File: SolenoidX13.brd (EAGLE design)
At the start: 24.3 x 25.4 mm, 23 parts, among them U1 ULN2003V12

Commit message: big pog uwu
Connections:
- net SWCLK: now also STM.PA14; no longer STM.PA13
- net SWDIO: now also STM.PA13; no longer STM.PA14
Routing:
- net SWDIO: track 41.8 -> 43.2 mm
- net SWCLK: track 34.1 -> 34.8 mm
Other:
- board text added: "+3.3v"
- board text added: "GND"
- board text added: "NRST"
- board text added: "SWCLK"
- board text added: "SWDIO"
- board text added: "X13 Solenoid 5/14/21 Erin Park Katherine Sandys Grant Geyer"
- board text removed: "X13 Solenoid 01/01/2021 Erin Park Katherine Sandys Grant Geyer"
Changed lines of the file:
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@@
 3.3V
 STM</text>
-<text x="14.5288" y="0.6096" size="0.6096" layer="25">X13 Solenoid
-01/01/2021
+<text x="13.8938" y="0.4826" size="0.6096" layer="25">X13 Solenoid
+5/14/21
 Erin Park
 Katherine Sandys
@@
 <rectangle x1="17.789525" y1="9.336403125" x2="17.98764375" y2="9.352915625" layer="200"/>
 <rectangle x1="17.822546875" y1="9.352915625" x2="17.954621875" y2="9.369421875" layer="200"/>
+<text x="18.8468" y="0.6096" size="0.6096" layer="25">+3.3v</text>
+<text x="17.7038" y="3.2766" size="0.6096" layer="25">SWCLK</text>
+<text x="18.5928" y="5.9436" size="0.6096" layer="25">GND</text>
+<text x="17.7038" y="8.6106" size="0.6096" layer="25">SWDIO</text>
+<text x="18.3388" y="10.8966" size="0.6096" layer="25">NRST</text>
 </plain>
 <attributes>
@@
 <attribute name="MF" value="" x="22.0472" y="6.2738" size="1.778" layer="27" rot="R270" display="off"/>
 <attribute name="MPN" value="" x="22.0472" y="6.2738" size="1.778" layer="27" rot="R270" display="off"/>
-<attribute name="NAME" x="19.7866" y="11.4808" size="0.8128" layer="25" ratio="10" rot="R270"/>
+<attribute name="NAME" x="18.3642" y="11.7856" size="0.8128" layer="25" ratio="10"/>
 <attribute name="OC_FARNELL" value="unknown" x="22.0472" y="6.2738" size="1.778" layer="27" rot="R270" display="off"/>
 <attribute name="OC_NEWARK" value="unknown" x="22.0472" y="6.2738" size="1.778" layer="27" rot="R270" display="off"/>
@@
 <via x="19.1798" y="10.414" extent="1-16" drill="0.35"/>
 <via x="14.176" y="4.0386" extent="1-16" drill="0.35"/>
-<via x="15.827" y="9.4742" extent="1-16" drill="0.35"/>
+<via x="16.208" y="9.2202" extent="1-16" drill="0.35"/>
 <via x="6.8862" y="6.5024" extent="1-16" drill="0.35"/>
 <contactref element="RESET" pad="1"/>
@@
 <wire x1="22.0472" y1="8.7982125" x2="15.5444" y2="2.2954125" width="0.254" layer="1"/>
 <wire x1="22.0472" y1="8.8138" x2="22.0472" y2="8.7982125" width="0.254" layer="1"/>
-<wire x1="22.0472" y1="8.8138" x2="22.0472" y2="8.9408" width="0.254" layer="1"/>
-<wire x1="19.4474" y1="11.5406" x2="22.0472" y2="8.9408" width="0.254" layer="1"/>
 <contactref element="U$1" pad="13"/>
 <wire x1="0.4826" y1="10.1854" x2="1.1572" y2="10.86" width="0.2032" layer="16"/>
 <wire x1="1.1572" y1="10.86" x2="2.286" y2="10.86" width="0.2032" layer="16"/>
-<contactref element="STM" pad="PA14"/>
-<wire x1="17.6142" y1="11.5406" x2="19.4474" y2="11.5406" width="0.254" layer="1"/>
+<contactref element="STM" pad="PA13"/>
+<wire x1="16.8142" y1="11.5406" x2="16.8142" y2="10.7448" width="0.254" layer="1"/>
+<wire x1="19.177" y1="9.144" x2="19.431" y2="9.398" width="0.254" layer="1"/>
+<wire x1="19.431" y1="9.398" x2="21.463" y2="9.398" width="0.254" layer="1"/>
+<wire x1="21.463" y1="9.398" x2="22.0472" y2="8.8138" width="0.254" layer="1"/>
+<wire x1="16.8142" y1="10.7448" x2="18.415" y2="9.144" width="0.254" layer="1"/>
+<wire x1="18.415" y1="9.144" x2="19.177" y2="9.144" width="0.254" layer="1"/>
 </signal>
 <signal name="SWCLK">
 <contactref element="SV1" pad="4"/>
-<via x="17.442890625" y="10.381690625" extent="1-16" drill="0.35"/>
-<wire x1="17.442890625" y1="10.381690625" x2="17.2692" y2="10.208" width="0.2032" layer="16"/>
 <via x="10.318" y="9.7076875" extent="1-16" drill="0.35"/>
 <wire x1="12.525" y1="10.5636" x2="11.9359125" y2="10.5636" width="0.2032" layer="16"/>
 <wire x1="11.9359125" y1="10.5636" x2="11.08" y2="9.7076875" width="0.2032" layer="16"/>
 <wire x1="11.08" y1="9.7076875" x2="10.318" y2="9.7076875" width="0.2032" layer="16"/>
-<wire x1="17.2692" y1="10.208" x2="12.8806" y2="10.208" width="0.2032" layer="16"/>
-<wire x1="12.8806" y1="10.208" x2="12.525" y2="10.5636" width="0.2032" layer="16"/>
+<wire x1="17.2692" y1="10.589" x2="16.6342" y2="9.954" width="0.2032" layer="16"/>
+<wire x1="16.6342" y1="9.954" x2="13.1346" y2="9.954" width="0.2032" layer="16"/>
+<wire x1="13.1346" y1="9.954" x2="12.525" y2="10.5636" width="0.2032" layer="16"/>
 <wire x1="10.318" y1="9.7076875" x2="9.1488875" y2="9.7076875" width="0.2032" layer="1"/>
 <wire x1="9.1488875" y1="9.7076875" x2="7.2898" y2="7.8486" width="0.2032" layer="1"/>
-<wire x1="17.442890625" y1="10.381690625" x2="20.4216" y2="7.40298125" width="0.254" layer="16"/>
 <wire x1="20.4216" y1="5.3594" x2="22.0472" y2="3.7338" width="0.254" layer="16"/>
-<wire x1="20.4216" y1="7.40298125" x2="20.4216" y2="5.3594" width="0.254" layer="16"/>
+<wire x1="20.4216" y1="5.3594" x2="20.4216" y2="8.16498125" width="0.254" layer="16"/>
 <contactref element="U$1" pad="11"/>
 <wire x1="7.2898" y1="7.8486" x2="1.1684" y2="7.8486" width="0.2032" layer="1"/>
@@
 <wire x1="1.43" y1="12.86" x2="2.286" y2="12.86" width="0.2032" layer="1"/>
 <wire x1="0.508" y1="11.938" x2="1.43" y2="12.86" width="0.2032" layer="1"/>
-<contactref element="STM" pad="PA13"/>
-<wire x1="16.8142" y1="11.5406" x2="16.8142" y2="11.01038125" width="0.254" layer="1"/>
-<wire x1="16.8142" y1="11.01038125" x2="17.442890625" y2="10.381690625" width="0.254" layer="1"/>
+<contactref element="STM" pad="PA14"/>
+<wire x1="20.4216" y1="8.16498125" x2="18.12458125" y2="10.462" width="0.254" layer="16"/>
+<wire x1="18.12458125" y1="10.462" x2="17.99758125" y2="10.589" width="0.2032" layer="16"/>
+<wire x1="17.99758125" y1="10.589" x2="17.2692" y2="10.589" width="0.2032" layer="16"/>
+<wire x1="17.6142" y1="11.5406" x2="17.7412" y2="11.4136" width="0.254" layer="1"/>
+<wire x1="17.7412" y1="11.4136" x2="17.7412" y2="10.84538125" width="0.254" layer="1"/>
+<wire x1="18.12458125" y1="10.462" x2="17.7412" y2="10.84538125" width="0.254" layer="1"/>
+<via x="18.12458125" y="10.462" extent="1-16" drill="0.35"/>
 </signal>
 <signal name="SOL1_1">

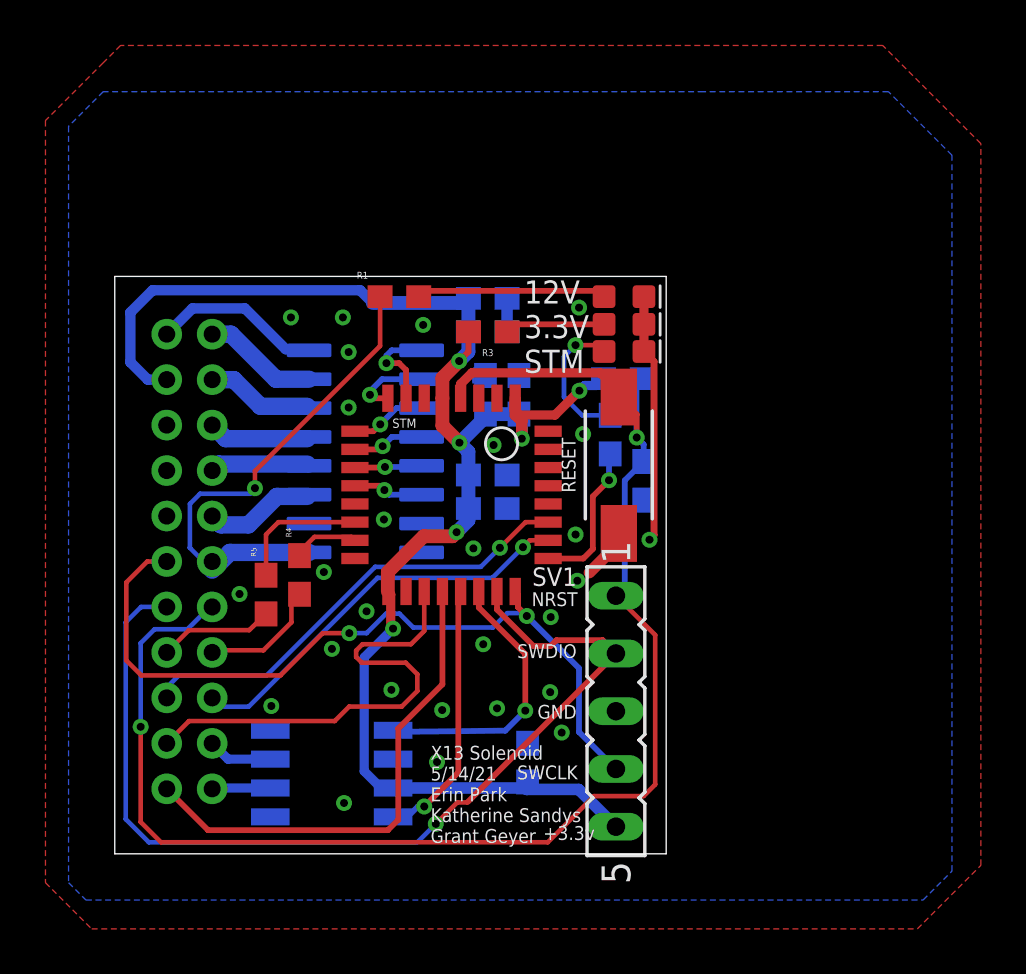
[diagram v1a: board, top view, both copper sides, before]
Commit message: New SWD programming connecotr
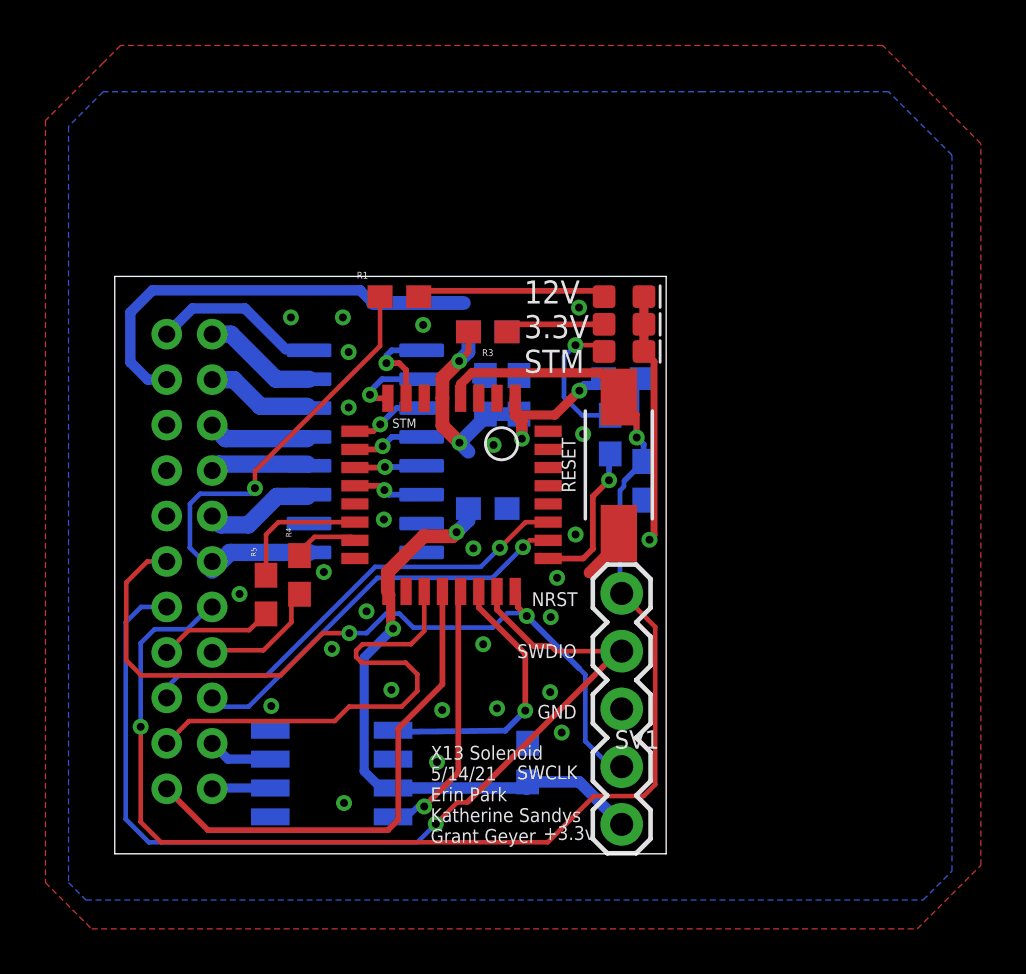
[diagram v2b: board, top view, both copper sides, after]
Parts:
- removed C4, C6: 4.7uF, SparkFun-Capacitors:0603
- C10, C2, C3, C5, C7: value 4.7uF -> 0.1uF
- R2: value 1k -> 10k
- SV1: value (none) -> 3V3 -SWCLK-GND-SWDIO- NRST; device con-lsta:FE05-1 -> CONN, Serial Wire Programming Headers:1X05
- moved SV1 4.98 mm to (22.3, 1.30), turned to 90 degrees
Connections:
- net +3V3: now also SV1.1; no longer C4.1, C6.1, SV1.5
- net GND: no longer C4.2, C6.2
- net NRST: now also SV1.5; no longer SV1.1
- net SWCLK: now also SV1.2; no longer SV1.4
- net SWDIO: now also SV1.4; no longer SV1.2
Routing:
- net +3V3: track 69.0 -> 65.1 mm
- net GND: track 14.7 -> 13.2 mm

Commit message: wack
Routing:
- net +3V3: track 65.1 -> 66.3 mm
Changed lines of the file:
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@@
 </polygon>
 <via x="19.4592" y="12.1412" extent="1-16" drill="0.35"/>
-<via x="19.1798" y="10.414" extent="1-16" drill="0.35"/>
+<via x="20.0688" y="10.287" extent="1-16" drill="0.35"/>
 <via x="14.176" y="4.0386" extent="1-16" drill="0.35"/>
 <via x="16.208" y="9.2202" extent="1-16" drill="0.35"/>
@@
 <via x="11.8392" y="14.7066" extent="1-16" drill="0.35"/>
 <via x="16.6652" y="17.9832" extent="1-16" drill="0.35"/>
-<via x="19.1544" y="7.112" extent="1-16" drill="0.35"/>
+<via x="19.9164" y="7.366" extent="1-16" drill="0.35"/>
 <wire x1="23.2798" y1="22.098" x2="23.7236" y2="21.6542" width="0.3048" layer="1"/>
 <wire x1="22.1742" y1="14.0942" x2="22.1742" y2="13.6652" width="0.3048" layer="1"/>
@@
 <wire x1="23.7236" y1="14.018" x2="23.5232" y2="13.8176" width="0.3048" layer="1"/>
 <wire x1="23.7236" y1="21.6542" x2="23.7236" y2="14.018" width="0.3048" layer="1"/>
-<wire x1="23.2798" y1="24.511" x2="20.4244" y2="24.0284" width="0" layer="19" extent="1-1"/>
-<wire x1="22.1742" y1="14.0942" x2="23.5232" y2="13.8176" width="0" layer="19" extent="1-1"/>
-<wire x1="19.4592" y1="12.1412" x2="20.8788" y2="12.3698" width="0" layer="19" extent="1-1"/>
-<wire x1="23.2664" y1="15.5584" x2="23.5232" y2="13.8176" width="0" layer="19" extent="16-16"/>
-<wire x1="19.1798" y1="10.414" x2="19.4592" y2="12.1412" width="0" layer="19" extent="1-1"/>
-<wire x1="20.272" y1="14.0462" x2="20.8788" y2="12.3698" width="0" layer="19" extent="1-1"/>
-<wire x1="17.2584" y1="15.1892" x2="20.272" y2="14.0462" width="0" layer="19" extent="16-16"/>
-<wire x1="15.7762" y1="13.4366" x2="17.2584" y2="15.1892" width="0" layer="19" extent="16-16"/>
-<wire x1="13.4986" y1="13.2588" x2="15.7762" y2="13.4366" width="0" layer="19" extent="16-16"/>
-<wire x1="11.8392" y1="14.7066" x2="13.4986" y2="13.2588" width="0" layer="19" extent="16-16"/>
-<wire x1="10.5642" y1="12.9906" x2="11.8392" y2="14.7066" width="0" layer="19" extent="1-1"/>
-<wire x1="9.1976" y1="12.3952" x2="10.5642" y2="12.9906" width="0" layer="19" extent="1-1"/>
-<wire x1="11.0772" y1="10.668" x2="10.5642" y2="12.9906" width="0" layer="19" extent="1-1"/>
 <wire x1="9.5532" y1="9.017" x2="11.0772" y2="10.668" width="0" layer="19" extent="1-1"/>
-<wire x1="16.6652" y1="17.9832" x2="17.2584" y2="15.1892" width="0" layer="19" extent="16-16"/>
-<wire x1="19.0642" y1="17.7906" x2="16.6652" y2="17.9832" width="0" layer="19" extent="1-1"/>
-<wire x1="19.0642" y1="18.5906" x2="19.0642" y2="17.7906" width="0" layer="19" extent="1-1"/>
-<wire x1="20.6022" y1="18.4658" x2="19.0642" y2="18.5906" width="0" layer="19" extent="1-1"/>
-<wire x1="17.78" y1="21.043" x2="19.0642" y2="18.5906" width="0" layer="19" extent="1-16"/>
-<wire x1="16.3068" y1="21.043" x2="17.78" y2="21.043" width="0" layer="19" extent="16-16"/>
-<wire x1="17.2584" y1="22.9616" x2="17.78" y2="21.043" width="0" layer="19" extent="16-16"/>
-<wire x1="12.1694" y1="7.2136" x2="9.5532" y2="9.017" width="0" layer="19" extent="1-1"/>
-<wire x1="14.4046" y1="6.3246" x2="12.1694" y2="7.2136" width="0" layer="19" extent="1-1"/>
-<wire x1="14.176" y1="4.0386" x2="14.4046" y2="6.3246" width="0" layer="19" extent="1-1"/>
-<wire x1="12.2428" y1="4.1656" x2="14.176" y2="4.0386" width="0" layer="19" extent="16-16"/>
-<wire x1="16.8176" y1="6.4008" x2="14.4046" y2="6.3246" width="0" layer="19" extent="1-1"/>
-<wire x1="18.161" y1="4.8632" x2="16.8176" y2="6.4008" width="0" layer="19" extent="16-16"/>
-<wire x1="19.6624" y1="5.334" x2="18.161" y2="4.8632" width="0" layer="19" extent="16-16"/>
-<wire x1="19.1544" y1="7.112" x2="19.6624" y2="5.334" width="0" layer="19" extent="1-1"/>
-<wire x1="22.3012" y1="6.3754" x2="19.6624" y2="5.334" width="0" layer="19" extent="1-1"/>
-<wire x1="16.208" y1="9.2202" x2="16.8176" y2="6.4008" width="0" layer="19" extent="1-1"/>
-<wire x1="10.0866" y1="2.2352" x2="12.2428" y2="4.1656" width="0" layer="19" extent="16-16"/>
-<wire x1="13.5664" y1="23.2664" x2="16.3068" y2="21.043" width="0" layer="19" extent="16-16"/>
-<wire x1="10.2898" y1="22.0726" x2="13.5664" y2="23.2664" width="0" layer="19" extent="1-1"/>
-<wire x1="10.0358" y1="23.5966" x2="10.2898" y2="22.0726" width="0" layer="19" extent="1-1"/>
-<wire x1="7.7498" y1="23.5966" x2="10.0358" y2="23.5966" width="0" layer="19" extent="1-1"/>
-<wire x1="10.2898" y1="19.6342" x2="10.2898" y2="22.0726" width="0" layer="19" extent="1-1"/>
-<wire x1="6.8862" y1="6.5024" x2="9.5532" y2="9.017" width="0" layer="19" extent="1-1"/>
-<wire x1="5.4892" y1="11.43" x2="9.1976" y2="12.3952" width="0" layer="19" extent="1-1"/>
-<wire x1="2.286" y1="14.86" x2="5.4892" y2="11.43" width="0" layer="19" extent="1-1"/>
-<wire x1="2.286" y1="16.86" x2="2.286" y2="14.86" width="0" layer="19" extent="1-1"/>
-<wire x1="2.286" y1="18.86" x2="2.286" y2="16.86" width="0" layer="19" extent="1-1"/>
 </signal>
 <signal name="+3V3">
@@
 <via x="20.4401375" y="20.3736" extent="1-16" drill="0.35"/>
 <wire x1="10.795" y1="24.7904" x2="11.3538" y2="24.2316" width="0.4572" layer="16"/>
-<wire x1="11.3538" y1="24.2316" x2="15.3552" y2="24.2316" width="0.6096" layer="16"/>
 <wire x1="1.6628" y1="24.7904" x2="10.795" y2="24.7904" width="0.4572" layer="16"/>
 <wire x1="15.5584" y1="22.9616" x2="15.5584" y2="22.0832125" width="0.6096" layer="16"/>
@@
 <wire x1="0.6858" y1="21.6274" x2="1.4532" y2="20.86" width="0.4572" layer="16"/>
 <wire x1="1.4532" y1="20.86" x2="2.286" y2="20.86" width="0.4572" layer="16"/>
-<wire x1="18.161" y1="3.1632" x2="20.4334" y2="3.1632" width="0.508" layer="16"/>
-<wire x1="20.4334" y1="3.1632" x2="22.3012" y2="1.2954" width="0.508" layer="16"/>
-<wire x1="15.3552" y1="24.2316" x2="15.5584" y2="22.9616" width="0" layer="19" extent="16-16"/>
+<wire x1="18.161" y1="3.1632" x2="19.6714" y2="3.1632" width="0.508" layer="16"/>
+<wire x1="21.5392" y1="1.2954" x2="22.3012" y2="1.2954" width="0.508" layer="16"/>
+<wire x1="21.5392" y1="1.2954" x2="19.6714" y2="3.1632" width="0.508" layer="16"/>
+<wire x1="11.3538" y1="24.2316" x2="11.4554" y2="24.13" width="0.4064" layer="16"/>
+<wire x1="15.5584" y1="23.8116" x2="15.5584" y2="22.9616" width="0.4064" layer="16"/>
+<wire x1="11.4554" y1="24.13" x2="15.24" y2="24.13" width="0.4064" layer="16"/>
+<wire x1="15.24" y1="24.13" x2="15.5584" y2="23.8116" width="0.4064" layer="16"/>
 <wire x1="15.5584" y1="15.1892" x2="15.5584" y2="17.6902" width="0" layer="19" extent="16-16"/>
 </signal>
@@
 <wire x1="13.3124" y1="0.508" x2="14.1224" y2="1.318" width="0.2032" layer="16"/>
 <via x="14.1224" y="1.318" extent="1-16" drill="0.35"/>
-<wire x1="14.1224" y1="1.318" x2="15.0678" y2="2.2634" width="0.2032" layer="1"/>
-<wire x1="15.5123875" y1="2.2634" x2="15.0678" y2="2.2634" width="0.2032" layer="1"/>
-<wire x1="15.5123875" y1="2.2634" x2="15.5444" y2="2.2954125" width="0.2032" layer="1"/>
 <wire x1="0.4826" y1="1.524" x2="0.4826" y2="10.1854" width="0.2032" layer="16"/>
-<wire x1="22.164390625" y1="8.915403125" x2="15.5444" y2="2.2954125" width="0.254" layer="1"/>
-<wire x1="22.3012" y1="8.9154" x2="22.164390625" y2="8.915403125" width="0.254" layer="1"/>
 <contactref element="U$1" pad="13"/>
 <wire x1="0.4826" y1="10.1854" x2="1.1572" y2="10.86" width="0.2032" layer="16"/>
@@
 <contactref element="STM" pad="PA13"/>
 <wire x1="16.8142" y1="11.5406" x2="16.8142" y2="10.7448" width="0.254" layer="1"/>
-<wire x1="16.8142" y1="10.7448" x2="18.415" y2="9.144" width="0.254" layer="1"/>
-<wire x1="19.177" y1="9.144" x2="18.415" y2="9.144" width="0.254" layer="1"/>
-<wire x1="22.3012" y1="8.9154" x2="19.4056" y2="8.9154" width="0.2032" layer="1"/>
-<wire x1="19.4056" y1="8.9154" x2="19.177" y2="9.144" width="0.2032" layer="1"/>
+<wire x1="18.923" y1="8.636" x2="18.923" y2="2.413" width="0.254" layer="1"/>
+<wire x1="18.923" y1="2.413" x2="17.828" y2="1.318" width="0.254" layer="1"/>
+<wire x1="17.828" y1="1.318" x2="14.1224" y2="1.318" width="0.254" layer="1"/>
+<wire x1="16.8142" y1="10.7448" x2="18.923" y2="8.636" width="0.254" layer="1"/>
+<wire x1="22.3012" y1="8.9154" x2="20.2184" y2="8.9154" width="0.254" layer="1"/>
+<wire x1="20.2184" y1="8.9154" x2="19.939" y2="8.636" width="0.254" layer="1"/>
+<wire x1="19.939" y1="8.636" x2="18.923" y2="8.636" width="0.254" layer="1"/>
 </signal>
 <signal name="SWCLK">
@@
 <wire x1="0.508" y1="11.938" x2="1.43" y2="12.86" width="0.2032" layer="1"/>
 <contactref element="STM" pad="PA14"/>
-<wire x1="18.12458125" y1="10.462" x2="20.4216" y2="8.16498125" width="0.254" layer="16"/>
 <wire x1="18.12458125" y1="10.462" x2="17.99758125" y2="10.589" width="0.2032" layer="16"/>
 <wire x1="17.99758125" y1="10.589" x2="17.2692" y2="10.589" width="0.2032" layer="16"/>
@@
 <wire x1="18.12458125" y1="10.462" x2="17.7412" y2="10.84538125" width="0.254" layer="1"/>
 <via x="18.12458125" y="10.462" extent="1-16" drill="0.35"/>
-<wire x1="20.4216" y1="8.16498125" x2="20.701" y2="7.88558125" width="0.2032" layer="16"/>
-<wire x1="20.701" y1="7.88558125" x2="20.701" y2="4.953" width="0.2032" layer="16"/>
+<wire x1="20.701" y1="8.13958125" x2="20.701" y2="4.953" width="0.2032" layer="16"/>
 <wire x1="20.701" y1="4.953" x2="21.8186" y2="3.8354" width="0.2032" layer="16"/>
 <wire x1="21.8186" y1="3.8354" x2="22.3012" y2="3.8354" width="0.2032" layer="16"/>
+<wire x1="20.701" y1="8.13958125" x2="18.37858125" y2="10.462" width="0.2032" layer="16"/>
+<wire x1="18.37858125" y1="10.462" x2="18.12458125" y2="10.462" width="0.2032" layer="16"/>
 </signal>
 <signal name="SOL1_1">
